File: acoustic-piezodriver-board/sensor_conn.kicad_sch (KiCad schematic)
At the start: 14 parts, among them J501 Conn_02x06_Odd_Even, U401 AMS1117-3.3, U402 TMP102xxDRL, U403 TMP102xxDRL

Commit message: [schematic] added adc for temperature measurement, current sense resistors, [layout] component placement, connector placement
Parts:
- added C404: 0.1uF, Capacitor_SMD:C_0402_1005Metric, symbol Device:C_Small
- added R406: 0, Resistor_SMD:R_0603_1608Metric_Pad0.98x0.95mm_HandSolder, symbol Device:R_Small
- added R407, R408, R411: 10k, Resistor_SMD:R_0603_1608Metric, symbol Device:R_Small
- added R409, R410: R_Small, symbol Device:R_Small
- added U404: ADS1115IDGS, Package_SO:TSSOP-10_3x3mm_P0.5mm, symbol Analog_ADC:ADS1115IDGS
- J501: footprint Connector_PinHeader_2.54mm:PinHeader_2x06_P2.54mm_Horizontal -> Connector_PinHeader_2.54mm:PinHeader_2x06_P2.54mm_Vertical; LPN (none) -> C124388; MPN (none) -> B-2100S12P-B110
- R402: value 4.7k -> 0; footprint Resistor_SMD:R_0402_1005Metric -> Resistor_SMD:R_0603_1608Metric_Pad0.98x0.95mm_HandSolder; LPN 0402WGF4701TCE -> C15402; MPN C25900 -> 0603WAJ0000T5E
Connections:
- net +3V3: now also C404.1, U404.8 (VDD)
- net GND: now also J501.10 (Pin_10), J501.2 (Pin_2), C404.2, R407.1, R408.1, R410.2, R411.1, U404.3 (GND); no longer J501.5 (Pin_5), J501.7 (Pin_7), J501.8 (Pin_8), U403.4 (ADD0)
- net PSEPIC_EN: now also J501.7 (Pin_7); no longer J501.2 (Pin_2)
- net PWM.0_HI: now also J501.12 (Pin_12); no longer J501.11 (Pin_11)
- net PWM.0_LI: now also J501.11 (Pin_11); no longer J501.9 (Pin_9)
- net PWM.1_HI: now also J501.8 (Pin_8); no longer J501.12 (Pin_12)
- net PWM.1_LI: now also J501.9 (Pin_9); no longer J501.10 (Pin_10)
- net T_SCL: now also R406.2, U404.10 (SCL)
- net T_SDA: now also U404.9 (SDA)
- net at R402.1, U402.4 (ADD0): now also R408.2
- new net: R411.2, U404.1 (ADDR)
- new net: R406.1, R407.2, U403.4 (ADD0)
- new net: R409.2, R410.1
- new net +BATT: R409.1
- new net ADC_IDC: U404.6 (AIN2)
- new net ADC_IFPGA: U404.7 (AIN3)
- new net ADC_ITOT: U404.5 (AIN1)
- new net ADC_VBAT: U404.4 (AIN0)
- no-connect marks 0 -> 2
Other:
- note added: "- Differential -> Single-ended input - Buffering - Amplification (range 0.1 -> 2 Amps), increments of 0.01"
- note added: "- Differential -> Single-ended input - Buffering - Amplification (range 0.1 -> 7 Amps), increments of 0.01"
- note added: "- I2C-ADDRESS: 1001000 - 860 SPS, input multiplexer - PGA: +-256 mV .. +-6.144V"
- note added: "ADDRESS: 1001001"
- note added: "ADDRESS: 1001011"
- note added: "BATT measurement"
- note added: "CURRENT MEASUREMENT"
- note added: "IDC measurement"
- note added: "ITOT measurement"
- note added: "I_FPGA measurement"
- moved on the sheet: C401, C402, C403, D401, D402, J501, R401, R403, R404, R405, U401, U402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

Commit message: [piezodriver] Added resistive divider (next) come up with a solution for current sensing (galvanic isolation?)
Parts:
- removed R409, R410: R_Small, symbol Device:R_Small
- added R412: 200, Resistor_SMD:R_0402_1005Metric, symbol Device:R_Small
- added R413: 20k, Resistor_SMD:R_0402_1005Metric, symbol Device:R_Small
- added U405, U406, U407: OPA333xxDBV, Package_TO_SOT_SMD:SOT-23-5, symbol Amplifier_Operational:OPA333xxDBV
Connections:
- net +BATT: now also R413.1, U405.4 (-)
- net ADC_VBAT: now also R412.1, R413.2
- net BATT_P: now also U405.3 (+)
- net GND: now also R412.2
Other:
- note added: "- Differential -> Single-ended input - Buffering - Amplification (range 0.1 -> 5 Amps), increments of 0.01"
- note added: "- Differential -> Single-ended input - Buffering OPAMP - Amplification (range 0.1 -> 7 Amps), increments of 0.01"
- note added: "- R-divider: ratio 0.0099 - Vmax: 25 V -> 250 mV - Pmax: 62.5 mW - 25 V / 20e3 Ohm = 1.25 mA - 20e3 * (1.25e-3)**2 = 31.25 mW"
- note added: "OPAMP - PINS: OUT, Vs-, IN+, IN-, Vs+ - GBW: 350 kHz - Z_in = 3 MOhm (SE, +-275 mV) Figure 5: low-side current sensing circuit. - Issue: you might need to divide the voltages down somehow - Better idea: just do a single-ended and a differential measurement (check how high the inputs are actually allowed to go)"
- note removed: "- Differential -> Single-ended input - Buffering - Amplification (range 0.1 -> 7 Amps), increments of 0.01"
- moved on the sheet: C404, R411, U404

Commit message: found hal-sensor, replaced with different one for lower voltage signal source impedance, reorganised schematic
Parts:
- removed C402: 22uF, Capacitor_SMD:C_0805_2012Metric, symbol Device:C_Small
- removed U401: AMS1117-3.3, Package_TO_SOT_SMD:SOT-223-3_TabPin2, symbol Regulator_Linear:AMS1117-3.3
- removed U405, U406, U407: OPA333xxDBV, Package_TO_SOT_SMD:SOT-23-5, symbol Amplifier_Operational:OPA333xxDBV
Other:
- note added: "VBATT MEASUREMENT"
- note removed: "- Differential -> Single-ended input - Buffering - Amplification (range 0.1 -> 2 Amps), increments of 0.01"
- note removed: "- Differential -> Single-ended input - Buffering - Amplification (range 0.1 -> 5 Amps), increments of 0.01"
- note removed: "- Differential -> Single-ended input - Buffering OPAMP - Amplification (range 0.1 -> 7 Amps), increments of 0.01"
- note removed: "BATT measurement"
- note removed: "I_FPGA measurement"
- note removed: "OPAMP - PINS: OUT, Vs-, IN+, IN-, Vs+ - GBW: 350 kHz - Z_in = 3 MOhm (SE, +-275 mV) Figure 5: low-side current sensing circuit. - Issue: you might need to divide the voltages down somehow - Better idea: just do a single-ended and a differential measurement (check how high the inputs are actually allowed to go)"
- note removed: "Vin_max: 15V"
- moved on the sheet: C404, R411, R412, R413, U404

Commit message: added new notes + schematic component hal sensors
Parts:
- added C402, C405, C406: 220nF, Capacitor_SMD:C_0402_1005Metric, symbol Device:C_Small
- added R409, R410, R414: 1k, Resistor_SMD:R_0402_1005Metric, symbol Device:R_Small
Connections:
- net ADC_IBAT: now also R409.1
- net ADC_IFPGA: now also R414.1; no longer U404.7 (AIN3)
- net ADC_IINV: now also R410.1
- net GND: now also C402.2, C405.2, C406.2
- net ADC_IDC: no longer names the net of U404.6 (AIN2)
- net ADC_IDC: now also C405.1, R410.2
- net ADC_ITOT: no longer names the net of U404.5 (AIN1)
- net ADC_ITOT: now also C402.1, R409.2
- new net: C406.1, R414.2, U404.7 (AIN3)
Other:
- note added: "ADC: - Z_hall_src = 0.2-2 Ohm - 16-bit accuracy: Vrange / (2**(16-1)) - I_in_max = 7.5 A, Vo_max = 7.5 * 0.2 = 1.5 V - Z_ADC_diff = 2.4 MOhm (at 1.024 V) [Assume average current won't be much larger] - Vin: (-1.024, 1.024) V, 200 mV / A - Accuracy: 31.25 uV -> 31.25 / 200 = 0.156 mA - I_in_max = 11.5 A, Vo_max = 11.5 * 0.2 = 2.25 V - Z_ADC_diff = 4.9 MOhm - Vin: (-2.048, 2.048) V, 200 mV / A - Ac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"
- note removed: "IDC measurement"
- note removed: "ITOT measurement"
- moved on the sheet: C404, R411, R412, R413, U404

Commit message: finished schematic, routing
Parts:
- R412: value 200 -> 1k8; footprint Resistor_SMD:R_0402_1005Metric -> Resistor_SMD:R_0603_1608Metric; LPN C25087 -> C4177; MPN 0402WGF2000TCE -> 0603WAF1801T5E
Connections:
- net ADC_ALERT: now reaches J501.5 (Pin_5)
- net ADC_ALERT: now also U404.2 (ALERT/RDY)
- no-connect marks 2 -> 0
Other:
- note added: "- R-divider: ratio 0.0099 - Vmax: 25 V -> 2.064 V - Pmax: 62.5 mW - 25 V / 22e3 Ohm = 1.2 mA - 20e3 * (1.2e-3)**2 = 28.8 mW"
- note removed: "- R-divider: ratio 0.0099 - Vmax: 25 V -> 250 mV - Pmax: 62.5 mW - 25 V / 20e3 Ohm = 1.25 mA - 20e3 * (1.25e-3)**2 = 31.25 mW"
- moved on the sheet: C404
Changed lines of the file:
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@@
 		)
 	)
-	(text "- R-divider: ratio 0.0099\n	- Vmax: 25 V -> 250 mV\n- Pmax: 62.5 mW\n	- 25 V / 20e3 Ohm = 1.25 mA\n	- 20e3 * (1.25e-3)**2 = 31.25 mW"
+	(text "- R-divider: ratio 0.0099\n	- Vmax: 25 V -> 2.064 V\n- Pmax: 62.5 mW\n	- 25 V / 22e3 Ohm = 1.2 mA\n	- 20e3 * (1.2e-3)**2 = 28.8 mW"
 		(exclude_from_sim no)
 		(at 210.058 89.916 0)
@@
 	)
 	(junction
+		(at 101.6 173.99)
+		(diameter 0)
+		(color 0 0 0 0)
+	)
+	(junction
 		(at 101.6 207.01)
 		(diameter 0)
@@
 	)
 	(junction
-		(at 101.6 173.99)
-		(diameter 0)
-		(color 0 0 0 0)
-	)
-	(junction
 		(at 54.61 110.49)
 		(diameter 0)
@@
 		(color 0 0 0 0)
 	)
-	(no_connect
-		(at 91.44 189.23)
-	)
-	(no_connect
-		(at 147.32 101.6)
-	)
 	(bus_entry
 		(at 176.53 111.76)
@@
 	(wire
 		(pts
+			(xy 110.49 173.99) (xy 110.49 175.26)
+		)
+		(stroke
+			(width 0)
+			(type default)
+		)
+	)
+	(wire
+		(pts
 			(xy 101.6 208.28) (xy 101.6 207.01)
 		)
@@
 	(wire
 		(pts
+			(xy 134.62 101.6) (xy 147.32 101.6)
+		)
+		(stroke
+			(width 0)
+			(type default)
+		)
+	)
+	(wire
+		(pts
 			(xy 54.61 119.38) (xy 68.58 119.38)
 		)
@@
 	(wire
 		(pts
-			(xy 72.39 87.63) (xy 72.39 86.36)
+			(xy 110.49 181.61) (xy 110.49 180.34)
 		)
 		(stroke
@@
 	(wire
 		(pts
-			(xy 82.55 44.45) (xy 73.66 44.45)
+			(xy 72.39 87.63) (xy 72.39 86.36)
 		)
 		(stroke
@@
 	(wire
 		(pts
-			(xy 134.62 199.39) (xy 134.62 220.98)
+			(xy 82.55 44.45) (xy 73.66 44.45)
 		)
 		(stroke
@@
 	(wire
 		(pts
-			(xy 110.49 180.34) (xy 110.49 179.07)
+			(xy 134.62 199.39) (xy 134.62 220.98)
 		)
 		(stroke
@@
 	(wire
 		(pts
+			(xy 78.74 189.23) (xy 91.44 189.23)
+		)
+		(stroke
+			(width 0)
+			(type default)
+		)
+	)
+	(wire
+		(pts
 			(xy 82.55 58.42) (xy 82.55 59.69)
 		)
@@
 	(wire
 		(pts
+			(xy 101.6 173.99) (xy 101.6 181.61)
+		)
+		(stroke
+			(width 0)
+			(type default)
+		)
+	)
+	(wire
+		(pts
 			(xy 48.26 53.34) (xy 48.26 44.45)
 		)
@@
 	(wire
 		(pts
-			(xy 101.6 173.99) (xy 101.6 181.61)
-		)
-		(stroke
-			(width 0)
-			(type default)
-		)
-	)
-	(wire
-		(pts
 			(xy 49.53 102.87) (xy 52.07 102.87)
 		)
@@
 		)
 	)
+	(label "ADC_ALERT"
+		(at 134.62 101.6 0)
+		(effects
+			(font
+				(size 1.27 1.27)
+			)
+			(justify left bottom)
+		)
+	)
 	(label "ADC_VBAT"
 		(at 115.57 191.77 0)
@@
 		)
 	)
+	(label "ADC_ALERT"
+		(at 78.74 189.23 0)
+		(effects
+			(font
+				(size 1.27 1.27)
+			)
+			(justify left bottom)
+		)
+	)
 	(label "T_SDA"
 		(at 49.53 100.33 0)
@@
 	(symbol
 		(lib_id "power:GND")
-		(at 110.49 180.34 0)
+		(at 110.49 181.61 0)
 		(unit 1)
 		(exclude_from_sim no)
@@
 		(dnp no)
 		(property "Reference" "#PWR0416"
-			(at 110.49 186.69 0)
+			(at 110.49 187.96 0)
 			(effects
 				(font
@@
 		)
 		(property "Value" "GND"
-			(at 105.664 182.372 0)
+			(at 107.442 181.61 0)
 			(effects
 				(font
@@
 		)
 		(property "Footprint" ""
-			(at 110.49 180.34 0)
+			(at 110.49 181.61 0)
 			(effects
 				(font
@@
 		)
 		(property "Datasheet" ""
-			(at 110.49 180.34 0)
+			(at 110.49 181.61 0)
 			(effects
 				(font
@@
 		)
 		(property "Description" "Power symbol creates a global label with name \"GND\" , ground"
-			(at 110.49 180.34 0)
+			(at 110.49 181.61 0)
 			(effects
 				(font
@@
 			)
 		)
-		(property "Value" "200"
+		(property "Value" "1k8"
 			(at 257.81 109.2199 0)
 			(effects
@@
 			)
 		)
-		(property "Footprint" "Resistor_SMD:R_0402_1005Metric"
+		(property "Footprint" "Resistor_SMD:R_0603_1608Metric"
 			(at 255.27 107.95 0)
 			(effects
@@
 			)
 		)
-		(property "LPN" "C25087"
+		(property "LPN" "C4177"
 			(at 255.27 107.95 0)
 			(effects
@@
 			)
 		)
-		(property "MPN" "0402WGF2000TCE"
+		(property "MPN" "0603WAF1801T5E"
 			(at 255.27 107.95 0)
 			(effects
@@
 	(symbol
 		(lib_id "Device:C_Small")
-		(at 110.49 176.53 0)
+		(at 110.49 177.8 0)
 		(mirror y)
 		(unit 1)
@@
 		(dnp no)
 		(property "Reference" "C404"
-			(at 113.284 172.974 0)
+			(at 116.84 175.26 0)
 			(effects
 				(font
@@
 		)
 		(property "Value" "0.1uF"
-			(at 107.188 176.022 0)
+			(at 118.11 177.546 0)
 			(effects
 				(font
@@
 		)
 		(property "Footprint" "Capacitor_SMD:C_0402_1005Metric"
-			(at 110.49 176.53 0)
+			(at 110.49 177.8 0)
 			(effects
 				(font
@@
 		)
 		(property "Datasheet" "https://jlcpcb.com/api/file/downloadByFileSystemAccessId/8603345729432014848"
-			(at 110.49 176.53 0)
+			(at 110.49 177.8 0)
 			(effects
 				(font
@@
 		)
 		(property "Description" "Unpolarized capacitor, small symbol"
-			(at 110.49 176.53 0)
+			(at 110.49 177.8 0)
 			(effects
 				(font
@@
 		)
 		(property "LPN" "C307331"
-			(at 110.49 176.53 0)
+			(at 110.49 177.8 0)
 			(effects
 				(font
@@
 		)
 		(property "MPN" "CL05B104KB54PNC"
-			(at 110.49 176.53 0)
+			(at 110.49 177.8 0)
 			(effects
 				(font

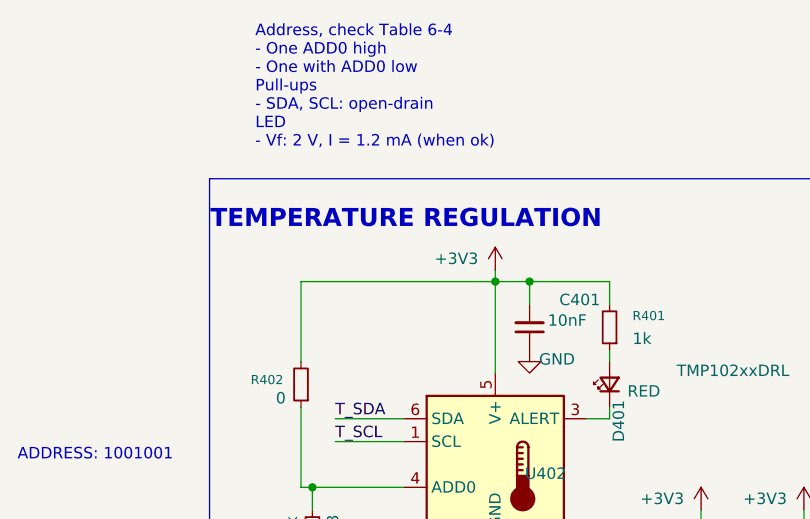
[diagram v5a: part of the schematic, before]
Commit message: Fixed ERC, DRC errors, finished routing (next) perform footprint checks
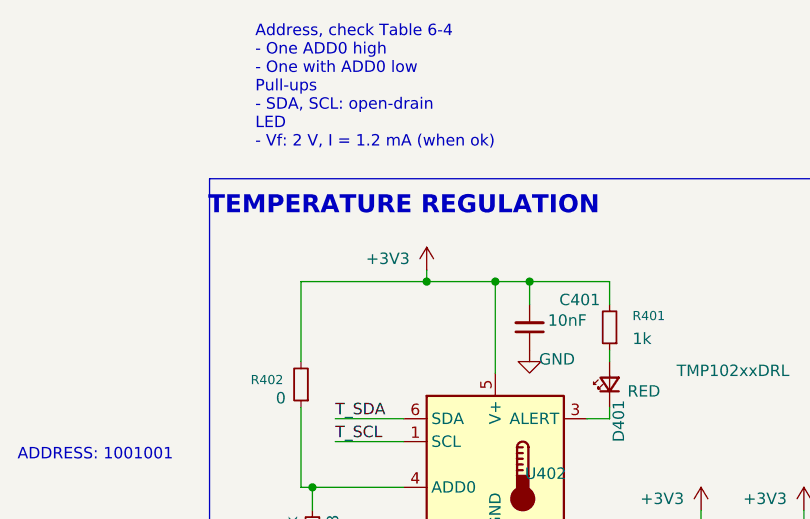
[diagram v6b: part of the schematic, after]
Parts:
- D401, D402: footprint Diode_SMD:D_0603_1608Metric -> LED_SMD:LED_0603_1608Metric
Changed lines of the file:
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@@
 	(text "TEMPERATURE REGULATION"
 		(exclude_from_sim no)
-		(at 59.944 37.592 0)
+		(at 59.69 36.068 0)
 		(effects
 			(font
@@
 		(color 0 0 0 0)
 	)
+	(junction
+		(at 62.23 44.45)
+		(diameter 0)
+		(color 0 0 0 0)
+	)
 	(bus_entry
 		(at 176.53 111.76)
@@
 	(wire
 		(pts
-			(xy 69.85 43.18) (xy 69.85 44.45)
+			(xy 62.23 43.18) (xy 62.23 44.45)
 		)
 		(stroke
@@
 	(wire
 		(pts
-			(xy 48.26 44.45) (xy 69.85 44.45)
+			(xy 48.26 44.45) (xy 62.23 44.45)
 		)
 		(stroke
@@
 	(wire
 		(pts
+			(xy 62.23 44.45) (xy 69.85 44.45)
+		)
+		(stroke
+			(width 0)
+			(type default)
+		)
+	)
+	(wire
+		(pts
 			(xy 92.71 69.85) (xy 92.71 72.39)
 		)
@@
 	(symbol
 		(lib_id "power:+3V3")
-		(at 69.85 43.18 0)
+		(at 62.23 43.18 0)
 		(unit 1)
 		(exclude_from_sim no)
@@
 		(dnp no)
 		(property "Reference" "#PWR0401"
-			(at 69.85 46.99 0)
+			(at 62.23 46.99 0)
 			(effects
 				(font
@@
 		)
 		(property "Value" "+3V3"
-			(at 65.532 41.91 0)
+			(at 57.912 41.91 0)
 			(effects
 				(font
@@
 		)
 		(property "Footprint" ""
-			(at 69.85 43.18 0)
+			(at 62.23 43.18 0)
 			(effects
 				(font
@@
 		)
 		(property "Datasheet" ""
-			(at 69.85 43.18 0)
+			(at 62.23 43.18 0)
 			(effects
 				(font
@@
 		)
 		(property "Description" "Power symbol creates a global label with name \"+3V3\""
-			(at 69.85 43.18 0)
+			(at 62.23 43.18 0)
 			(effects
 				(font
@@
 			)
 		)
-		(property "Footprint" "Diode_SMD:D_0603_1608Metric"
+		(property "Footprint" "LED_SMD:LED_0603_1608Metric"
 			(at 82.55 55.88 90)
 			(effects
@@
 			)
 		)
-		(property "Footprint" "Diode_SMD:D_0603_1608Metric"
+		(property "Footprint" "LED_SMD:LED_0603_1608Metric"
 			(at 81.28 96.52 90)
 			(effects

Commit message: [production checks] checked caps, [todo] Think about replacing 220 nF filtering caps in DC-DC to 0402 package (next) check rest of footprints
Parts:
- C401, C403: LCSC Part Number C15195 -> (none); LPN (none) -> C15195; MPN (none) -> CL05B103KB5NNNC
- R403, R404: LPN 0402WGF4701TCE -> C25900; MPN C25900 -> 0402WGF4701TCE
- R407, R408, R411: LPN 0603WAJ0103T5E -> C15401; MPN C15401 -> 0603WAJ0103T5E
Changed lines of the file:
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@@
 			)
 		)
-		(property "LCSC Part Number" "C15195"
+		(property "LPN" "C15195"
+			(at 73.66 49.53 0)
+			(effects
+				(font
+					(size 1.27 1.27)
+				)
+				(hide yes)
+			)
+		)
+		(property "MPN" "CL05B103KB5NNNC"
 			(at 73.66 49.53 0)
 			(effects
@@
 			)
 		)
-		(property "LPN" "0603WAJ0103T5E"
+		(property "LPN" "C15401"
 			(at 86.36 203.2 90)
 			(effects
@@
 			)
 		)
-		(property "MPN" "C15401"
+		(property "MPN" "0603WAJ0103T5E"
 			(at 86.36 203.2 90)
 			(effects
@@
 			)
 		)
-		(property "LPN" "0402WGF4701TCE"
+		(property "LPN" "C25900"
 			(at 92.71 74.93 90)
 			(effects
@@
 			)
 		)
-		(property "MPN" "C25900"
+		(property "MPN" "0402WGF4701TCE"
 			(at 92.71 74.93 90)
 			(effects
@@
 			)
 		)
-		(property "LPN" "0603WAJ0103T5E"
+		(property "LPN" "C15401"
 			(at 54.61 115.57 90)
 			(effects
@@
 			)
 		)
-		(property "MPN" "C15401"
+		(property "MPN" "0603WAJ0103T5E"
 			(at 54.61 115.57 90)
 			(effects
@@
 			)
 		)
-		(property "LPN" "0603WAJ0103T5E"
+		(property "LPN" "C15401"
 			(at 49.53 72.39 90)
 			(effects
@@
 			)
 		)
-		(property "MPN" "C15401"
+		(property "MPN" "0603WAJ0103T5E"
 			(at 49.53 72.39 90)
 			(effects
@@
 			)
 		)
-		(property "LPN" "0402WGF4701TCE"
+		(property "LPN" "C25900"
 			(at 104.14 74.93 90)
 			(effects
@@
 			)
 		)
-		(property "MPN" "C25900"
+		(property "MPN" "0402WGF4701TCE"
 			(at 104.14 74.93 90)
 			(effects
@@
 			)
 		)
-		(property "LCSC Part Number" "C15195"
+		(property "LPN" "C15195"
 			(at 72.39 90.17 0)
 			(effects
+				(font
+					(size 1.27 1.27)
+				)
+				(hide yes)
+			)
+		)
+		(property "MPN" "CL05B103KB5NNNC"
+			(at 72.39 90.17 0)
+			(effects
